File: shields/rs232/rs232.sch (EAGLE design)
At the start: 28 parts, among them Q5 2.5A/30V/105mΩ, Q6 2.5A/30V/105mΩ, Q7 2.5A/30V/105mΩ, Q8 2.5A/30V/105mΩ, U2 MAX3232, U3 OPENMV3

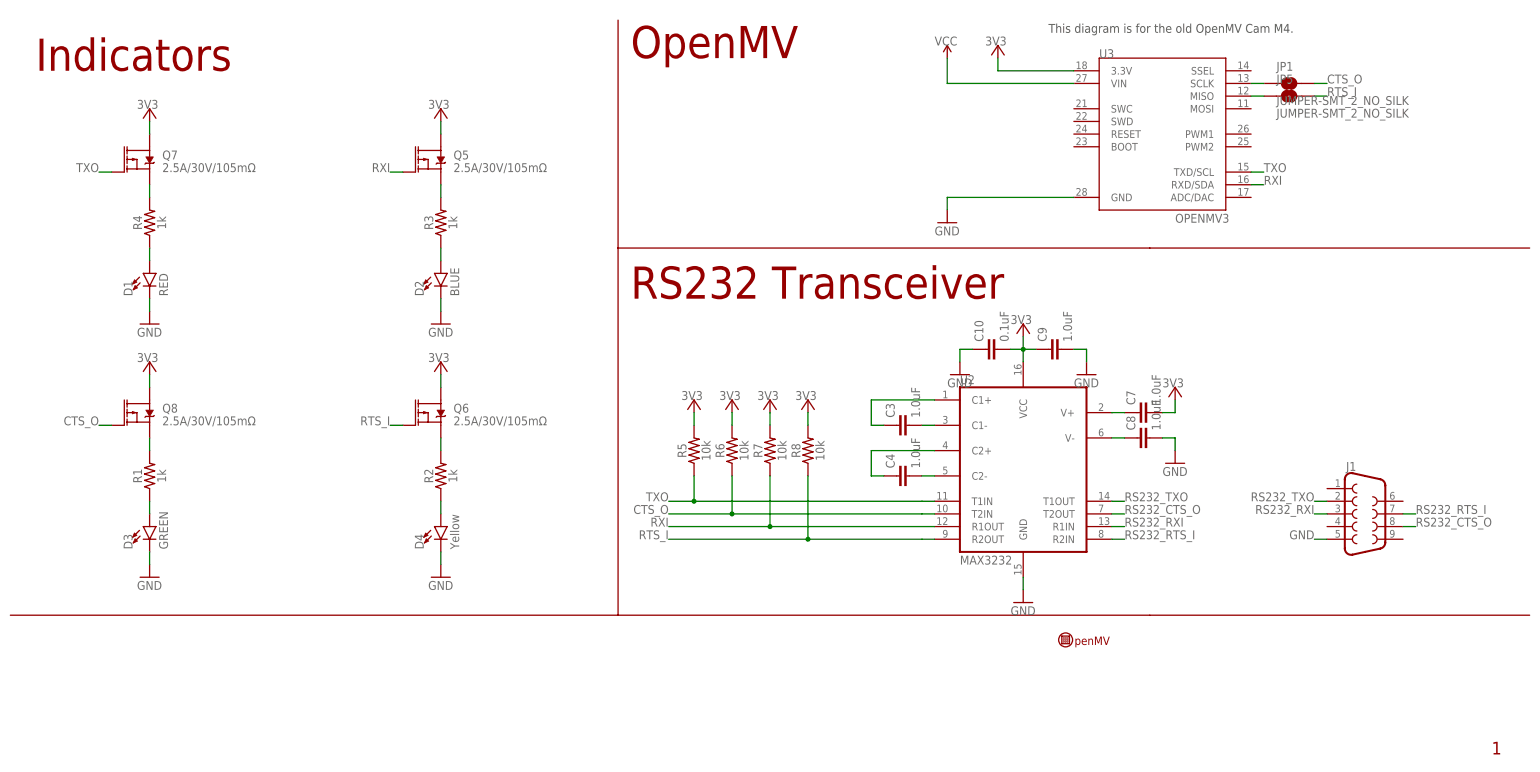
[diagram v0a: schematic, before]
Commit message: Fix rs232 shield
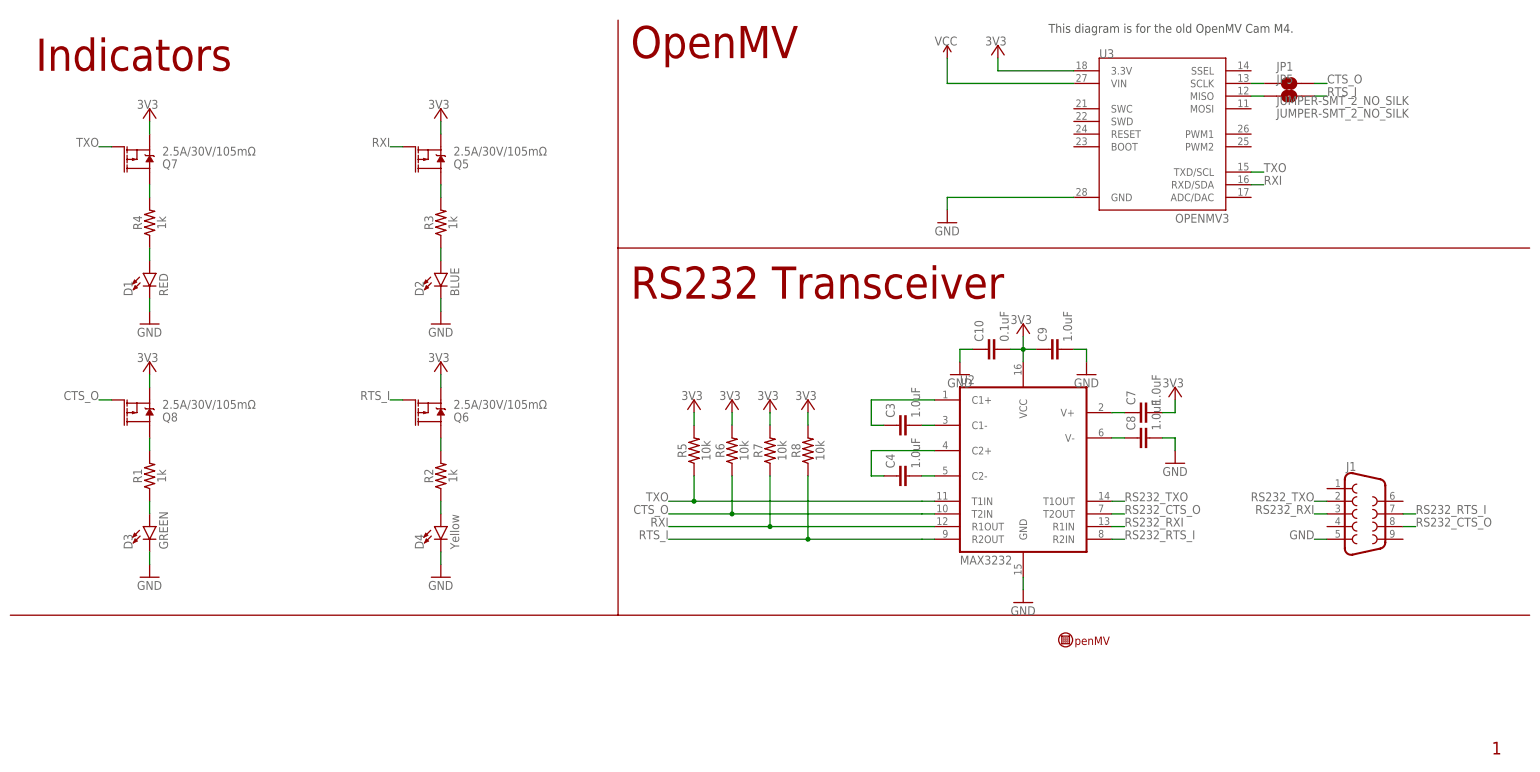
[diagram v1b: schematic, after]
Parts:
- J1: device SparkFun-Connectors:DB9MALE -> SparkFun-Connectors:DB9FEMALE
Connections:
- net 3V3: now also Q5.S, Q6.S, Q7.S, Q8.S; no longer Q5.D, Q6.D, Q7.D, Q8.D
- net N$10: now also Q8.D; no longer Q8.S
- net N$6: now also Q7.D; no longer Q7.S
- net N$7: now also Q5.D; no longer Q5.S
- net N$8: now also Q6.D; no longer Q6.S
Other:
- moved on the sheet: Q5, Q6, Q7, Q8
